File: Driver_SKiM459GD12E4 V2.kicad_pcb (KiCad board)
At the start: 4 copper layers, 169.2 x 116 mm, 339 parts, among them J1 2-338069-0, J13 EL1, J14 GL1, J15 NTC1_A, J16 NTC1_B, J17 GH1, J18 OUT1, J19 CH1, J20 EL2, J21 GL2, J22 NTC2_A, J23 NTC2_B, J24 GH2, J25 OUT2, J26 CH2, J27 EL3, J28 GL3, J29 NTC3_A, J30 NTC3_B, J31 GH3, J32 OUT3, J33 CH3, Q1 MJD44H11T4G, Q10 MJD45H11T4G, Q11 MJD44H11T4G, Q12 MJD45H11T4G, Q2 MJD45H11T4G, Q3 MJD44H11T4G, Q4 MJD45H11T4G, Q5 MJD44H11T4G, Q6 MJD45H11T4G, Q7 MJD44H11T4G, Q8 MJD45H11T4G, Q9 MJD44H11T4G, U1 LM2904, U2 R-785.0-1.0, U3 LM397, U4 HCPL-0611

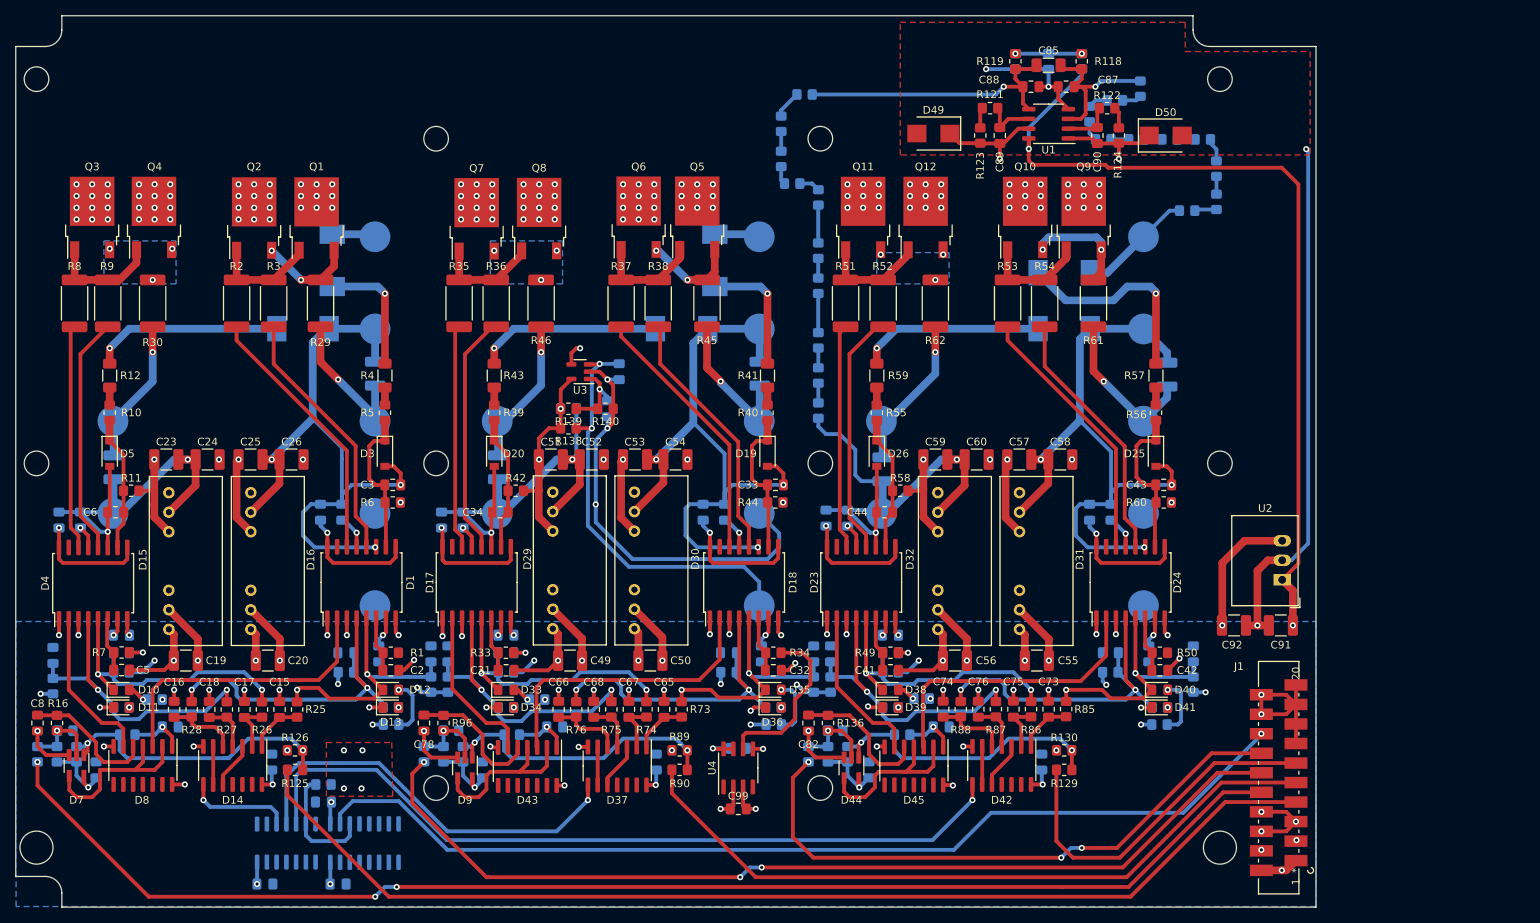
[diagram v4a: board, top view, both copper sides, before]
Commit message: Добавил сброс по температуре на все драйвера
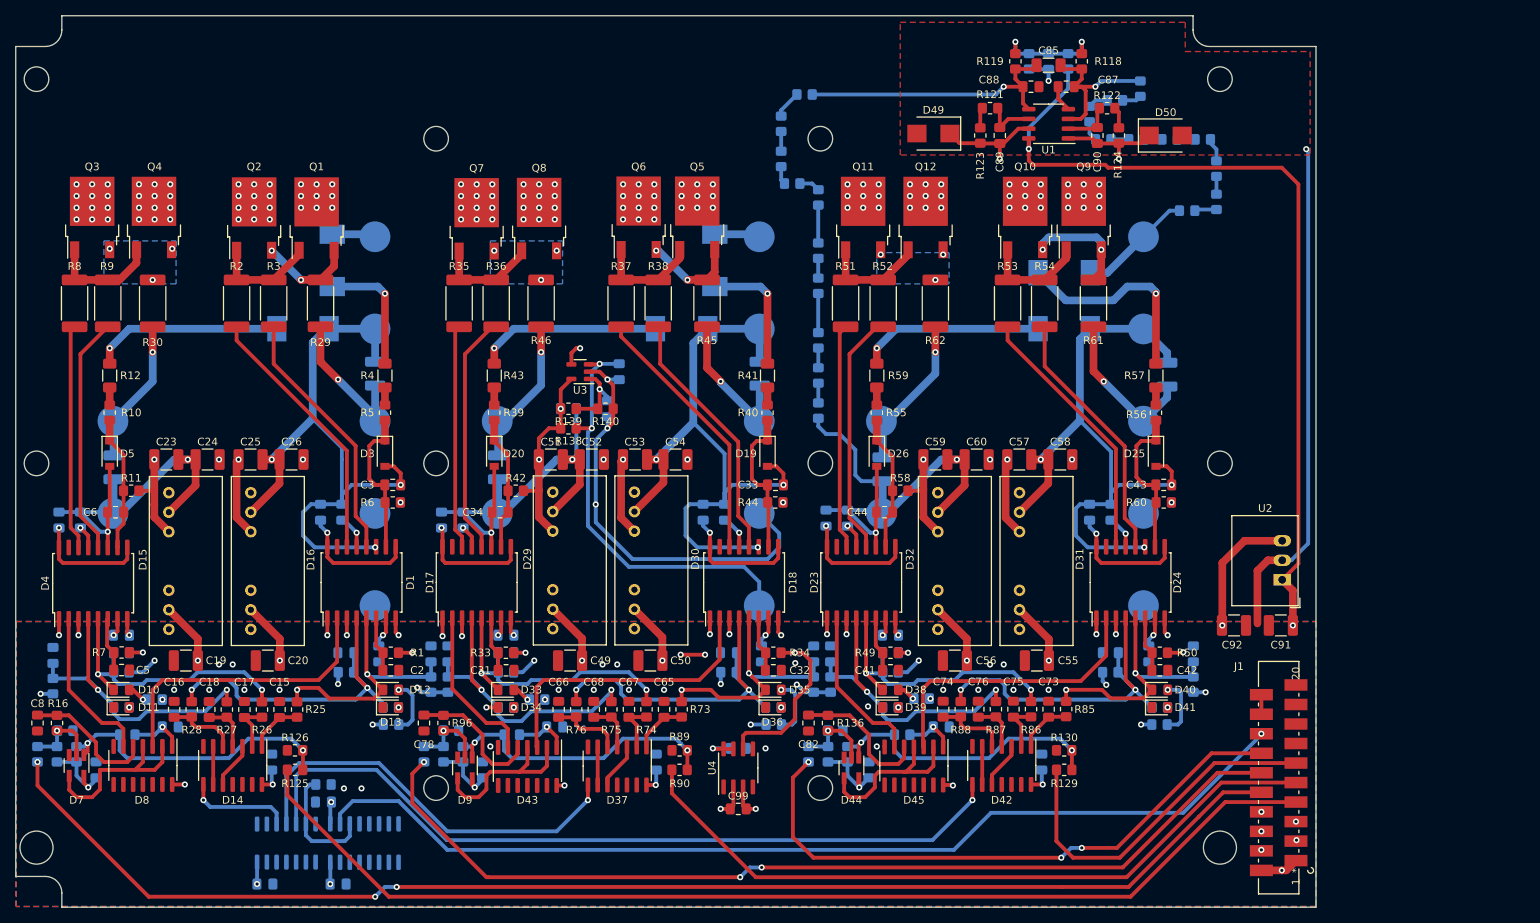
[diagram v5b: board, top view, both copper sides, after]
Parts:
- moved R113 1.78 mm to (192.0, 40.9)
- moved R114 1.78 mm to (197.1, 40.9)
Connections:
- R1 pad 1: RST_H1 -> RST_H3
- R33 pad 1: RST_L2 -> RST_H3
- R34 pad 1: RST_H2 -> RST_H3
- R49 pad 1: RST_L3 -> RST_H3
- R7 pad 1: RST_L1 -> RST_H3
- U4 pad 6: RST_H2 -> RST_H3
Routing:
- net GND: track 360.2 -> 190.3 mm, vias 71 -> 49
- net RST_H3: track 0.00 -> 167.8 mm, vias 0 -> 8
- net RST_H2: track 22.0 -> 0.00 mm
- net Net-(C86-Pad2): track 8.67 -> 14.2 mm
- net RST_L1: track 1.81 -> 0.00 mm, vias 1 -> 0
- net RST_L2: track 1.56 -> 0.00 mm, vias 1 -> 0
- net RST_L3: track 1.29 -> 0.00 mm, vias 1 -> 0
- net +15V: track 168.5 -> 167.7 mm
